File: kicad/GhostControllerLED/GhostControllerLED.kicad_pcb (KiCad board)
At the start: 2 copper layers, 28.3 x 28.3 mm, 16 parts, among them J1 Female LED Connector (No USB)

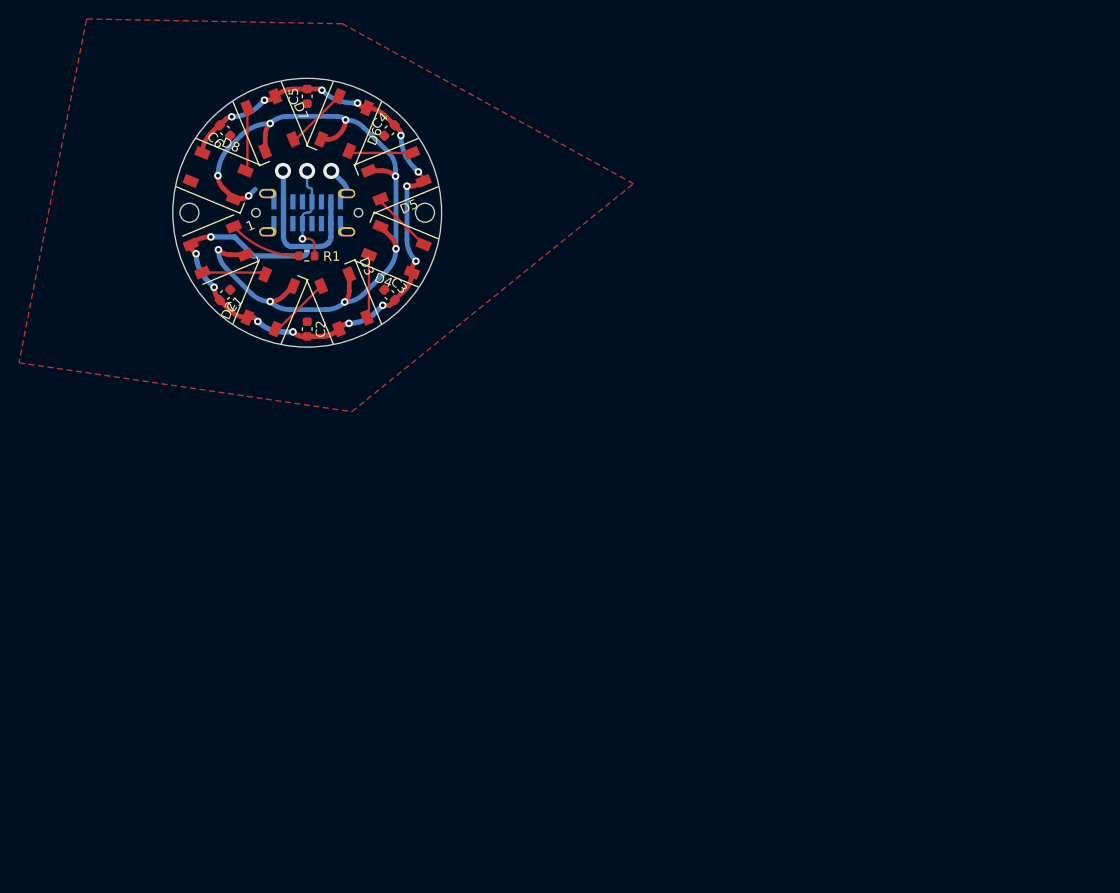
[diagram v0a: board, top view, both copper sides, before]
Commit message: chore: add copper fill zones
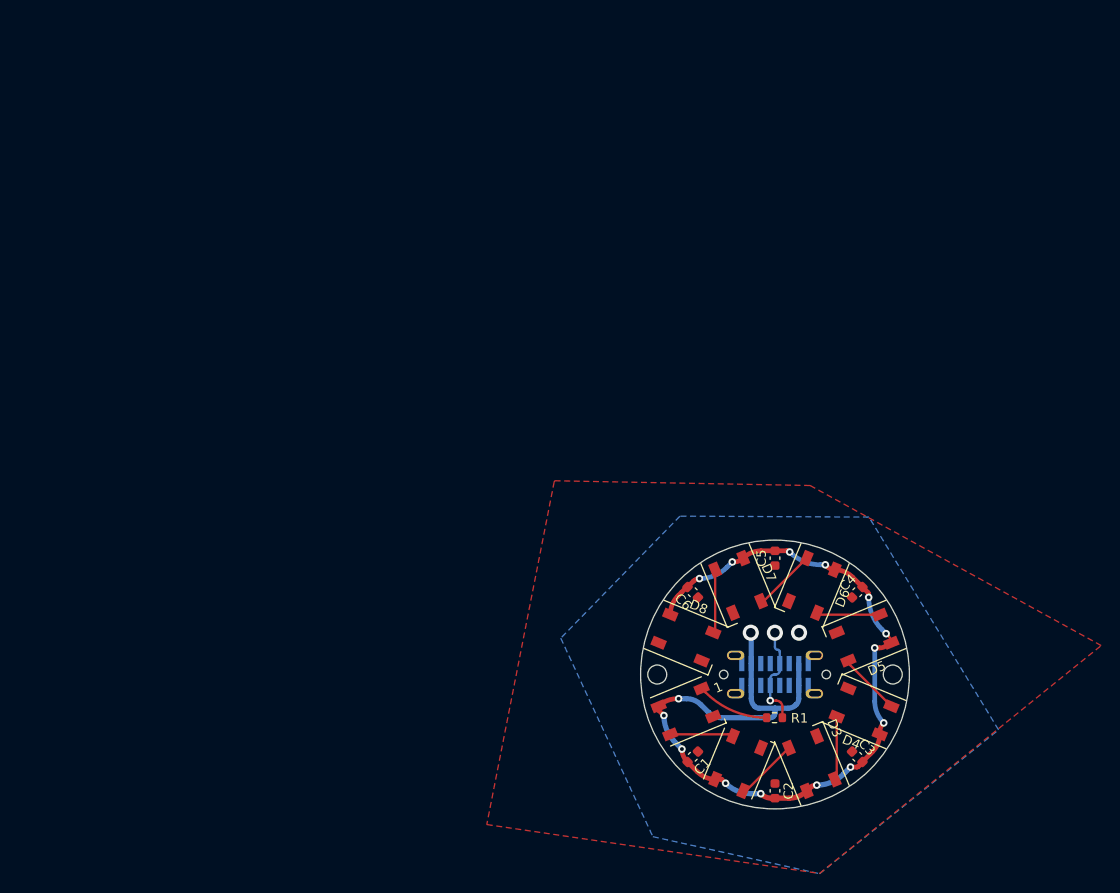
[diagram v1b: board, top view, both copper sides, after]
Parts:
- moved C2 69.2 mm to (49.3, 60.9)
- moved C5 69.2 mm to (49.3, 36.4)
- moved D2 69.2 mm to (45.4, 58.0)
- moved D4 69.2 mm to (58.6, 52.5)
- moved D5 69.2 mm to (58.6, 44.8)
- moved D7 69.2 mm to (45.4, 39.3)
- moved J1 69.2 mm to (49.3, 48.6)
- moved 1 69.2 mm to (39.9, 52.5)
- moved C1 69.2 mm to (40.6, 57.3)
- moved C3 69.2 mm to (57.9, 57.3)
- moved C4 69.2 mm to (57.9, 40.0)
- moved C6 69.2 mm to (40.6, 40.0)
- moved D3 69.2 mm to (53.2, 58.0)
- moved D6 69.2 mm to (53.2, 39.3)
- moved D8 69.2 mm to (39.9, 44.8)
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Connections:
- 1 pad 1: Net-(D1-VSS) -> GND
- D2 pad 1: Net-(D1-VSS) -> GND
- D3 pad 1: Net-(D1-VSS) -> GND
- D4 pad 1: Net-(D1-VSS) -> GND
- D5 pad 1: Net-(D1-VSS) -> GND
- D6 pad 1: Net-(D1-VSS) -> GND
- D6 pad 2: Net-(D6-DOUT) -> Net-(D5-DOUT)
- D6 pad 4: Net-(D5-DOUT) -> Net-(D6-DOUT)
- D7 pad 1: Net-(D1-VSS) -> GND
- D7 pad 2: Net-(D7-DOUT) -> Net-(D6-DOUT)
- D7 pad 4: Net-(D6-DOUT) -> Net-(D7-DOUT)
- D8 pad 1: Net-(D1-VSS) -> GND
- J1 pad 1: Net-(D1-VSS) -> GND
- J1 pad 2: (no net) -> GND
- J1 pad 3: (no net) -> GND
- J1 pad A1: Net-(D1-VSS) -> GND
- J1 pad A12: unconnected-(J1-GND-PadA12) -> GND
- J1 pad B1: unconnected-(J1-GND-PadB1) -> GND
- J1 pad B12: Net-(D1-VSS) -> GND
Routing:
- net Net-(D1-VSS): track 87.9 -> 0.00 mm, vias 10 -> 0
- net GND: track 0.00 -> 0.07 mm, vias 0 -> 1
- added copper zone on B.Cu, net GND
- added copper zone on F.Cu, net GND
- removed copper zone on F.Cu, net Net-(D1-VSS)
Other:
- outline, holes or cut-outs redrawn

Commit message: feat: finalize LED board design to 1.0
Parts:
- added G***: LOGO, LEDswarm:GhostIcon, B.Cu at (49.3, 39.0)
- added REF**: PinHeader_1x03_P2.54mm_Vertical, Connector_PinHeader_2.54mm:PinHeader_1x03_P2.54mm_Vertical, B.Cu at (46.7, 44.4)
- moved R1 0.61 mm to (49.2, 53.8)
- renumbered J1 to NoUSB
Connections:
- D2 pad 2: Net-(D2-DOUT) -> Net-(D1-DOUT)
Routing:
- net Net-(D1-VDD): track 106.1 -> 107.9 mm, vias 16 -> 15
- net Net-(J1-D+-PadA6): track 10.9 -> 11.5 mm, vias 2 -> 1
- net Net-(D1-DIN): track 7.69 -> 8.29 mm
- net GND: vias 1 -> 0
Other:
- board text added: "+5V"
- board text added: "D1"
- board text added: "D2"
- board text added: "D3"
- board text added: "D4"
- board text added: "D5"
- board text added: "D6"
- board text added: "D7"
- board text added: "D8"
- board text added: "DIN"
- board text added: "GND"
- board text added: "LEDswarm.com"
- board text added: "v1.0"
- board text added: "© 2024 Moritz Riede"
